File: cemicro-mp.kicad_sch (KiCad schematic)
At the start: 21 parts, among them U1 68HC11, U3 2764, U6 AMS1117-5.0

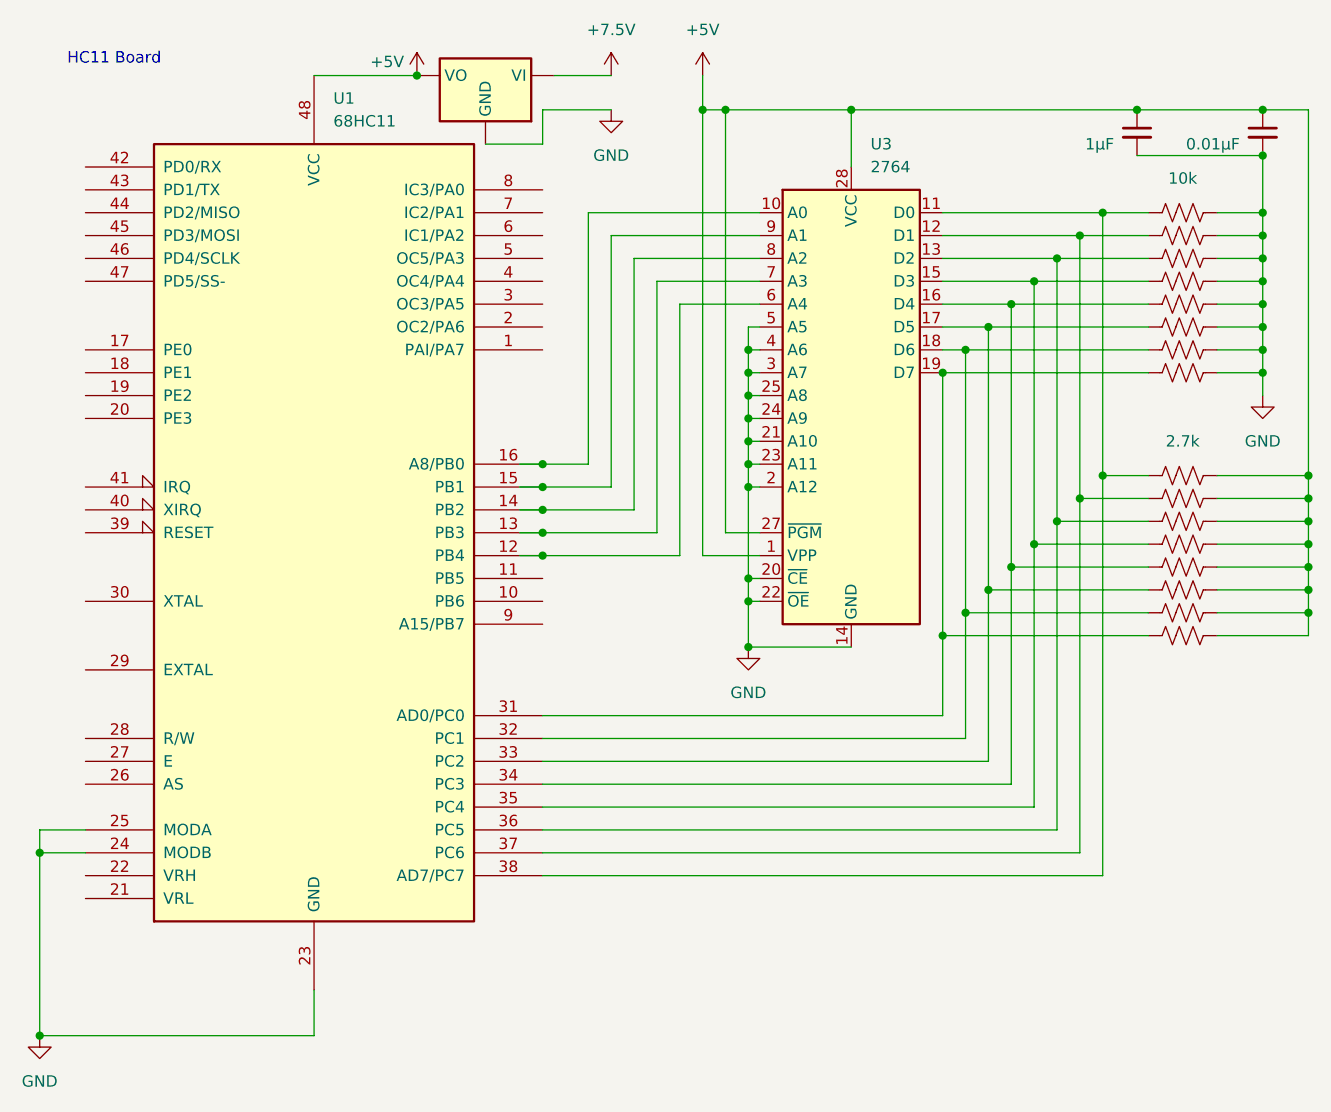
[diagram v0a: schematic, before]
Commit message: Fix reading from SCSR / Remove termination resistors from schematic
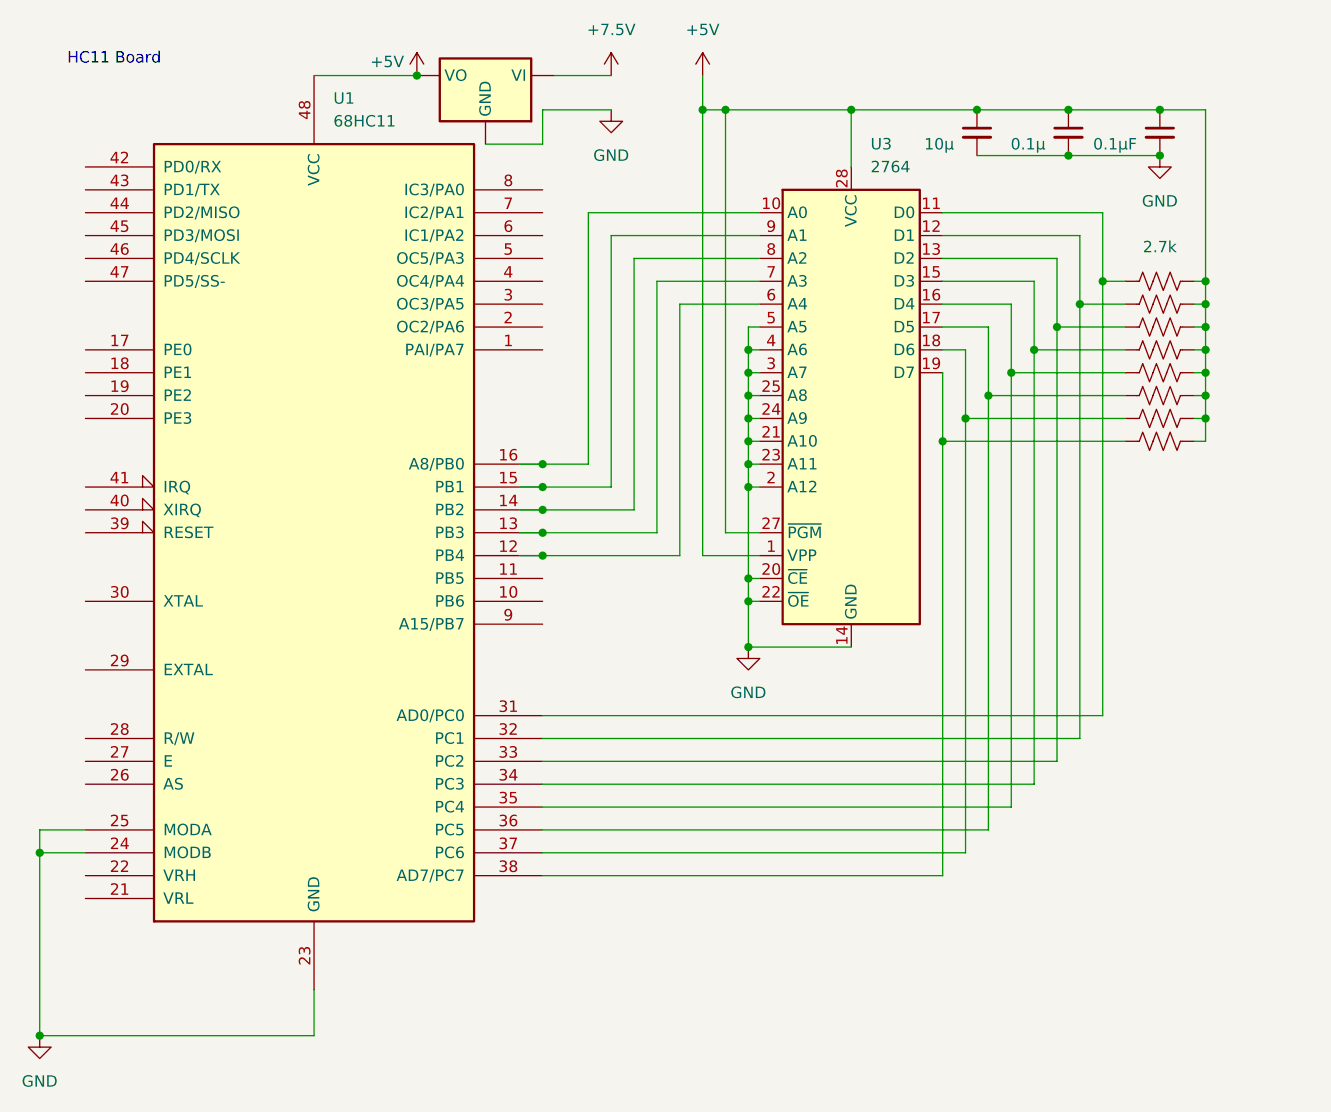
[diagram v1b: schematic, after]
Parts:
- removed R1, R2, R3, R4, R5, R6, R7, R8: 10k, symbol Device:R_US
- added C3: 10μ, symbol Device:C_Small
- C1: value 0.01μF -> 0.1μF
- C2: value 1μF -> 0.1μ
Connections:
- net +5V: now also C3.1
- net GND: now also C3.2
- net at R12.1, U3.15 (D3): now also U1.34 (PC3); no longer U1.35 (PC4)
- net at R16.1, U3.19 (D7): now also U1.38 (AD7/PC7); no longer U1.31 (AD0/PC0)
- net at R15.1, U3.18 (D6): now also U1.37 (PC6); no longer U1.32 (PC1)
- net at R14.1, U3.17 (D5): now also U1.36 (PC5); no longer U1.33 (PC2)
- net at R13.1, U3.16 (D4): now also U1.35 (PC4); no longer U1.34 (PC3)
- net at R11.1, U3.13 (D2): now also U1.33 (PC2); no longer U1.36 (PC5)
- net at R10.1, U3.12 (D1): now also U1.32 (PC1); no longer U1.37 (PC6)
- net at R9.1, U3.11 (D0): now also U1.31 (AD0/PC0); no longer U1.38 (AD7/PC7)

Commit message: Update schematic for PORTA connection
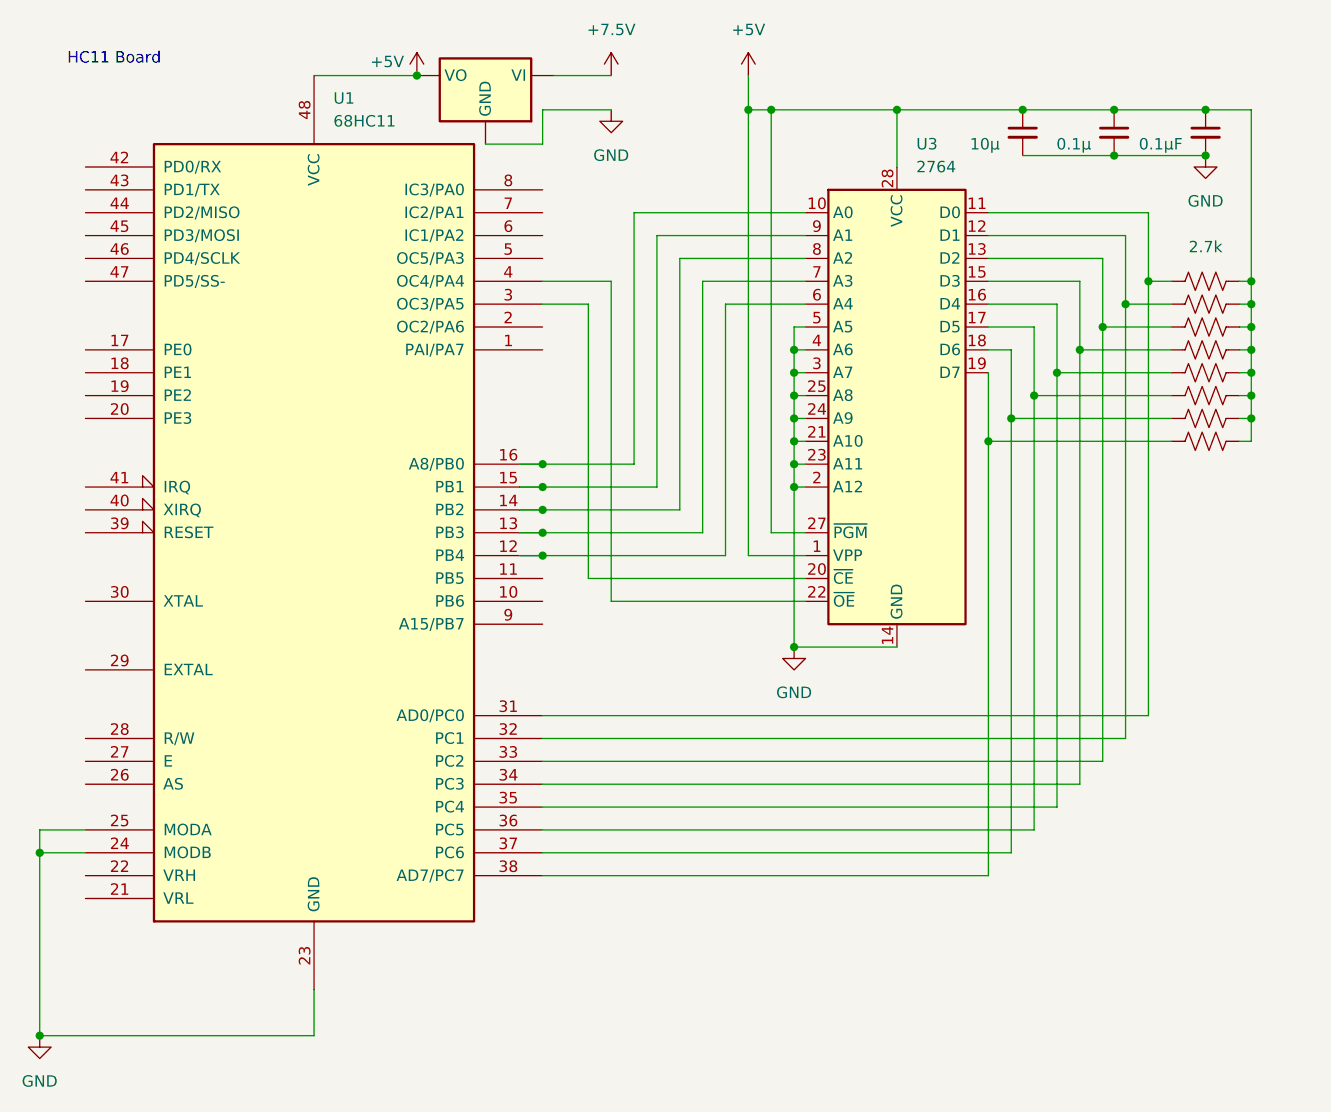
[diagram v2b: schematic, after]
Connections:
- net GND: no longer U3.20 (~{CE}), U3.22 (~{OE})
- net at U1.3 (OC3/PA5): now also U3.20 (~{CE})
- net at U1.4 (OC4/PA4): now also U3.22 (~{OE})
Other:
- moved on the sheet: U3
